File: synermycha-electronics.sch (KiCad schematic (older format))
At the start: 0 parts

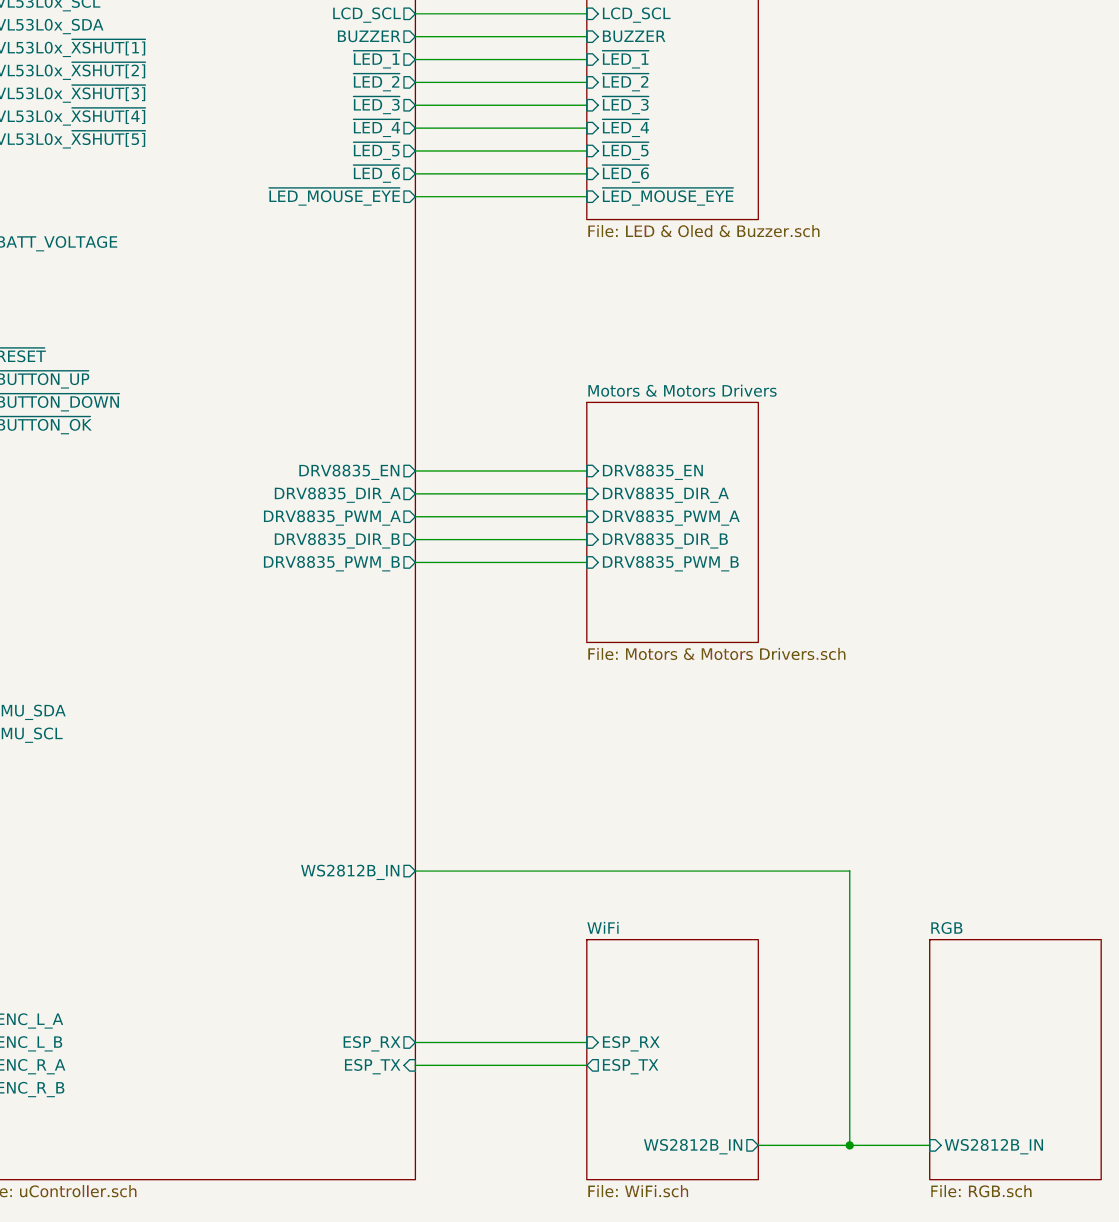
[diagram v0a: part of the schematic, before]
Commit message: Updated BT module connection, 3D models and wiring.
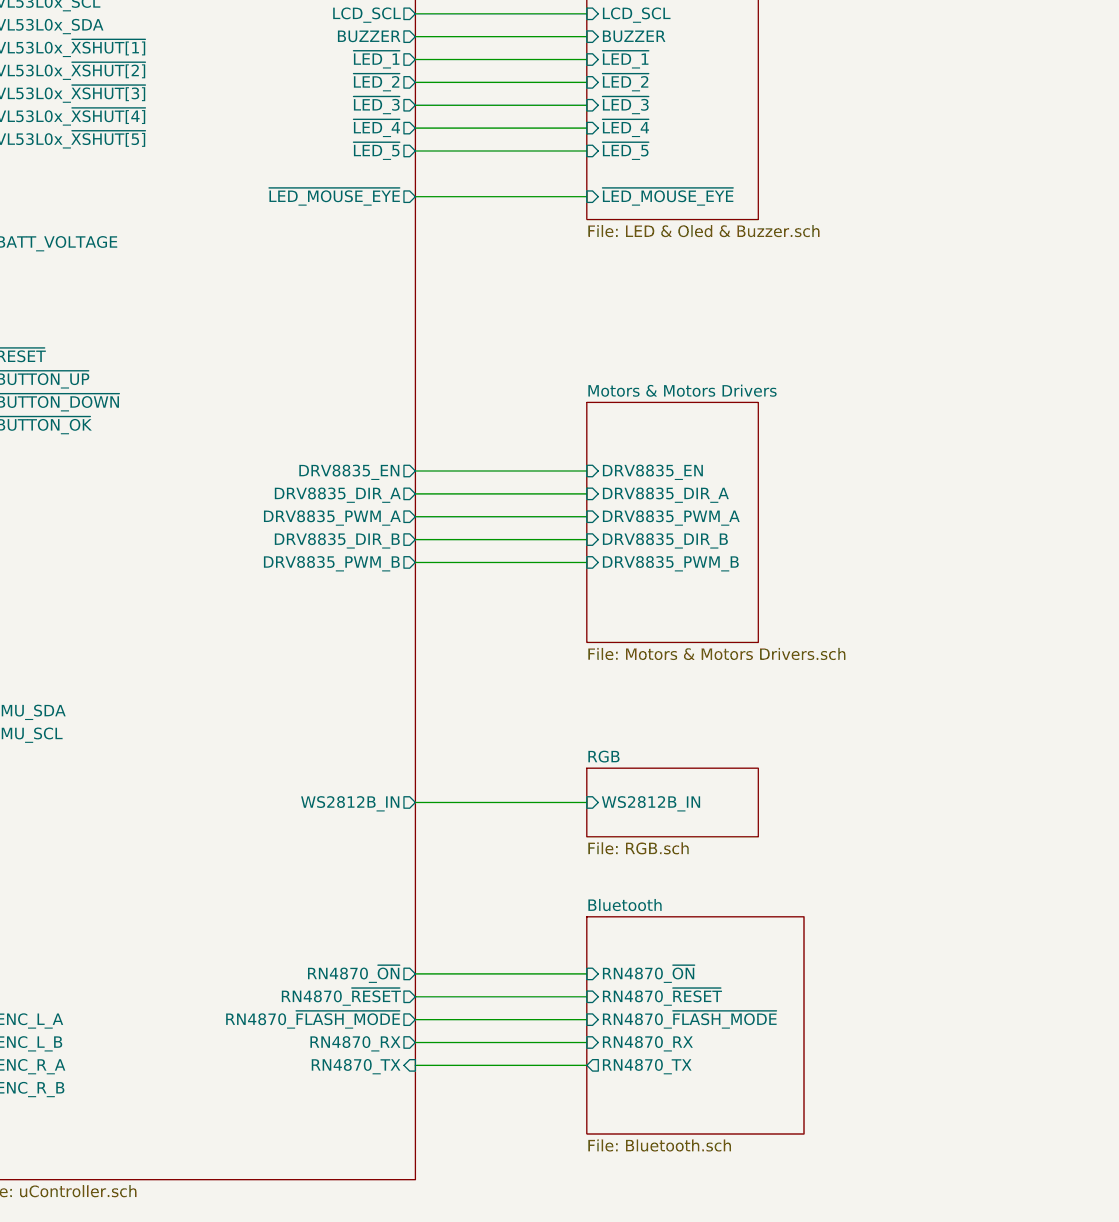
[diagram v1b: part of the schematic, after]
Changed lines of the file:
@@
 F8 "VL53L0x_~XSHUT[5]" I R 4050 1750 50
-$EndSheet
-$Sheet
-S 7350 5250 750  1050
-U 5E5F55AD
-F0 "WiFi" 50
-F1 "WiFi.sch" 50
-F2 "ESP_RX" I L 7350 5700 50
-F3 "ESP_TX" O L 7350 5800 50
-F4 "WS2812B_IN" O R 8100 6150 50
 $EndSheet
 Text Notes 1000 1150 0    50   ~ 0
@@
 F3 "IMU_SCL" I R 4050 4350 50
 $EndSheet
-$Sheet
-S 8850 5250 750  1050
-U 5E79B5DD
-F0 "RGB" 50
-F1 "RGB.sch" 50
-F2 "WS2812B_IN" I L 8850 6150 50
-$EndSheet
-Wire Wire Line
-	8100 6150 8500 6150
 Wire Wire Line
 	4050 2700 4700 2700
@@
 F15 "IMU_SDA" B L 4700 4250 50
 F16 "IMU_SCL" O L 4700 4350 50
-F17 "ESP_RX" O R 6600 5700 50
-F18 "ESP_TX" I R 6600 5800 50
+F17 "RN4870_RX" O R 6600 5700 50
+F18 "RN4870_TX" I R 6600 5800 50
 F19 "BATT_VOLTAGE" I L 4700 2200 50
 F20 "LCD_SDA" B R 6600 1100 50
@@
 F34 "VL53L0x_~XSHUT[4]" O L 4700 1650 50
 F35 "VL53L0x_~XSHUT[5]" O L 4700 1750 50
-F36 "~LED_6" O R 6600 1900 50
-F37 "WS2812B_IN" O R 6600 4950 50
+F36 "WS2812B_IN" O R 6600 4650 50
+F37 "RN4870_~ON" O R 6600 5400 50
+F38 "RN4870_~RESET" O R 6600 5500 50
+F39 "RN4870_~FLASH_MODE" O R 6600 5600 50
 $EndSheet
-Wire Wire Line
-	7350 1900 6600 1900
 Wire Wire Line
 	6600 1800 7350 1800
@@
 F9 "~LED_5" I L 7350 1800 50
 F10 "~LED_MOUSE_EYE" I L 7350 2000 50
-F11 "~LED_6" I L 7350 1900 50
 $EndSheet
 Wire Wire Line
@@
 Wire Wire Line
 	6600 2000 7350 2000
+$Sheet
+S 7350 4500 750  300
+U 5E79B5DD
+F0 "RGB" 50
+F1 "RGB.sch" 50
+F2 "WS2812B_IN" I L 7350 4650 50
+$EndSheet
 Wire Wire Line
-	6600 4950 8500 4950
+	7350 4650 6600 4650
+$Sheet
+S 7350 5150 950  950
+U 5E5F55AD
+F0 "Bluetooth" 50
+F1 "Bluetooth.sch" 50
+F2 "RN4870_RX" I L 7350 5700 50
+F3 "RN4870_TX" O L 7350 5800 50
+F4 "RN4870_~RESET" I L 7350 5500 50
+F5 "RN4870_~FLASH_MODE" I L 7350 5600 50
+F6 "RN4870_~ON" I L 7350 5400 50
+$EndSheet
 Wire Wire Line
-	8500 4950 8500 6150
-Connection ~ 8500 6150
+	7350 5600 6600 5600
 Wire Wire Line
-	8500 6150 8850 6150
+	6600 5500 7350 5500
+Wire Wire Line
+	7350 5400 6600 5400
 $EndSCHEMATC

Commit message: Zmieniono kontroler USB-PD
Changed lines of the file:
@@
 F1 "Power Section.sch" 50
 F2 "BATT_VOLTAGE" O R 1550 1350 50
+F3 "STSUSB4500_SDA" B R 1550 900 50
+F4 "STUSB_4500_SCL" I R 1550 1000 50
 $EndSheet
 $Sheet
@@
 F8 "VL53L0x_~XSHUT[5]" I R 4050 1750 50
 $EndSheet
-Text Notes 1000 1150 0    50   ~ 0
+Text Notes 650  1400 0    50   ~ 0
 6V,\n3V3\n
 $Sheet
@@
 Wire Wire Line
 	2450 2200 4700 2200
-Wire Wire Line
-	7350 1100 6600 1100
-Wire Wire Line
-	6600 1200 7350 1200
 $Sheet
 S 4700 950  1900 5350
@@
 Wire Wire Line
 	7350 5400 6600 5400
+Wire Wire Line
+	1550 1000 1750 1000
+Wire Wire Line
+	6600 1100 6900 1100
+Wire Wire Line
+	6800 800  6800 1200
+Wire Wire Line
+	6600 1200 6800 1200
+Connection ~ 6800 1200
+Wire Wire Line
+	6800 1200 7350 1200
+Wire Wire Line
+	6900 1100 6900 700
+Connection ~ 6900 1100
+Wire Wire Line
+	6900 1100 7350 1100
+Wire Wire Line
+	1550 900  1650 900
+Wire Wire Line
+	1650 700  1650 900
+Wire Wire Line
+	1650 700  6900 700
+Wire Wire Line
+	1750 1000 1750 800
+Wire Wire Line
+	1750 800  6800 800
 $EndSCHEMATC

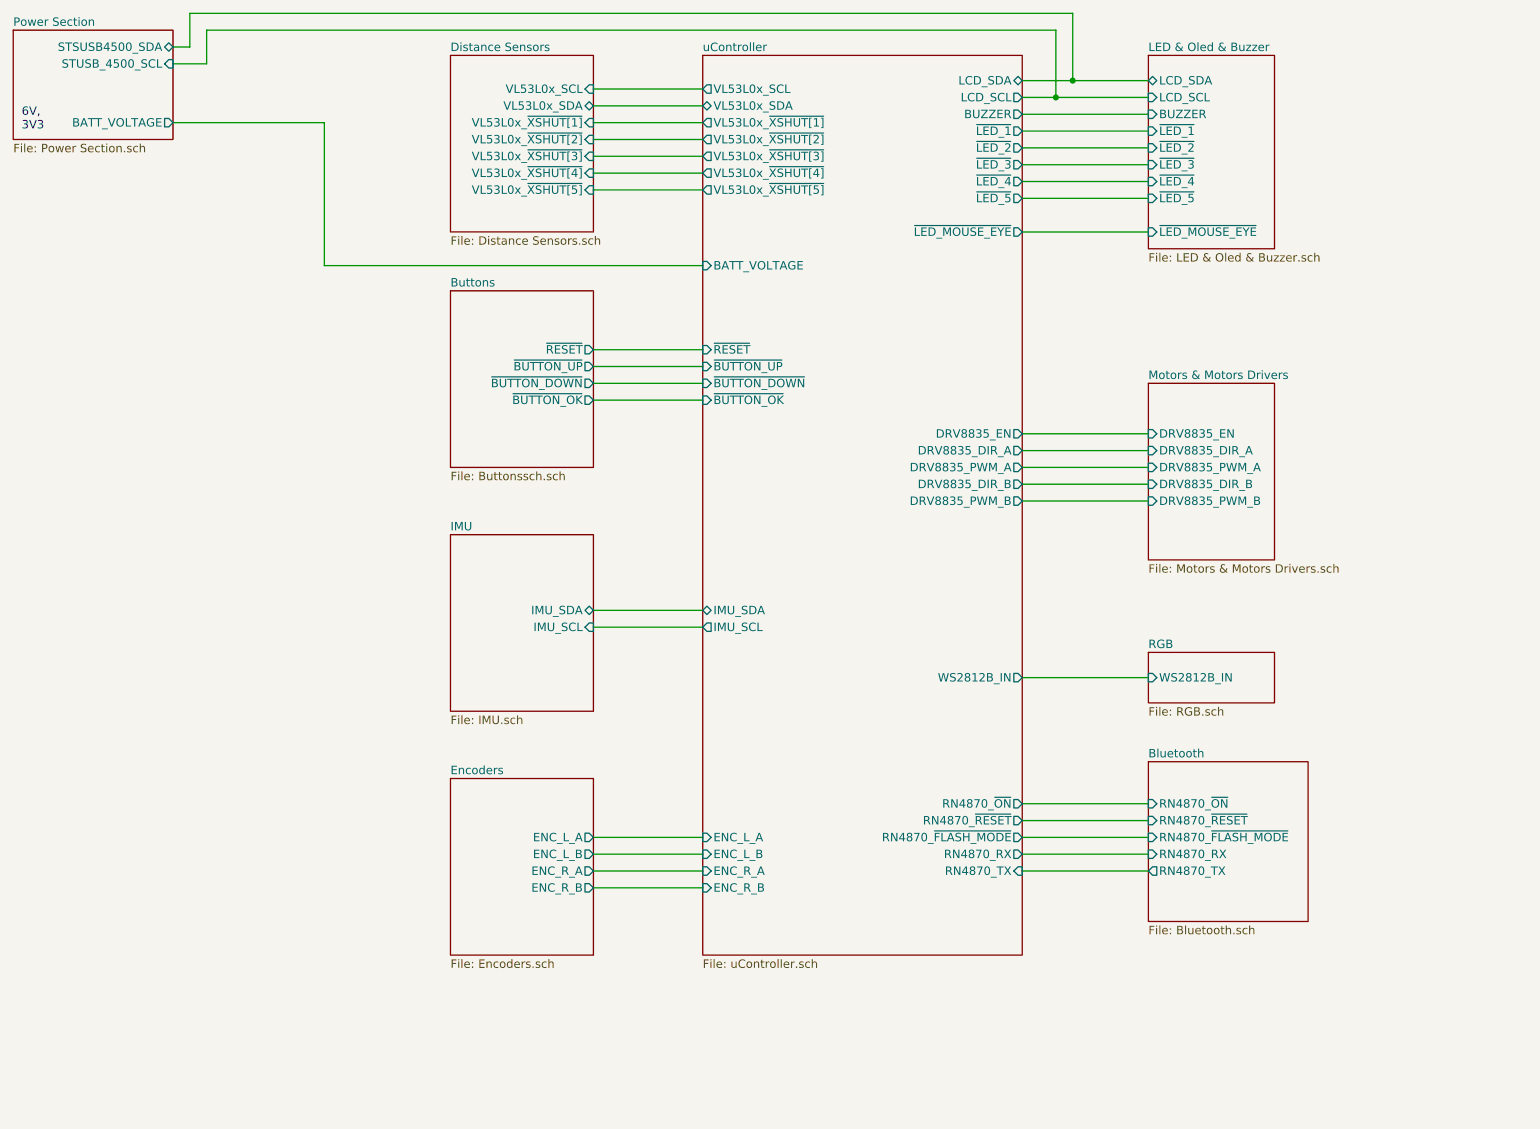
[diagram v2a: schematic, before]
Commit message: Dodano punkty testowe, poprawienie schematu
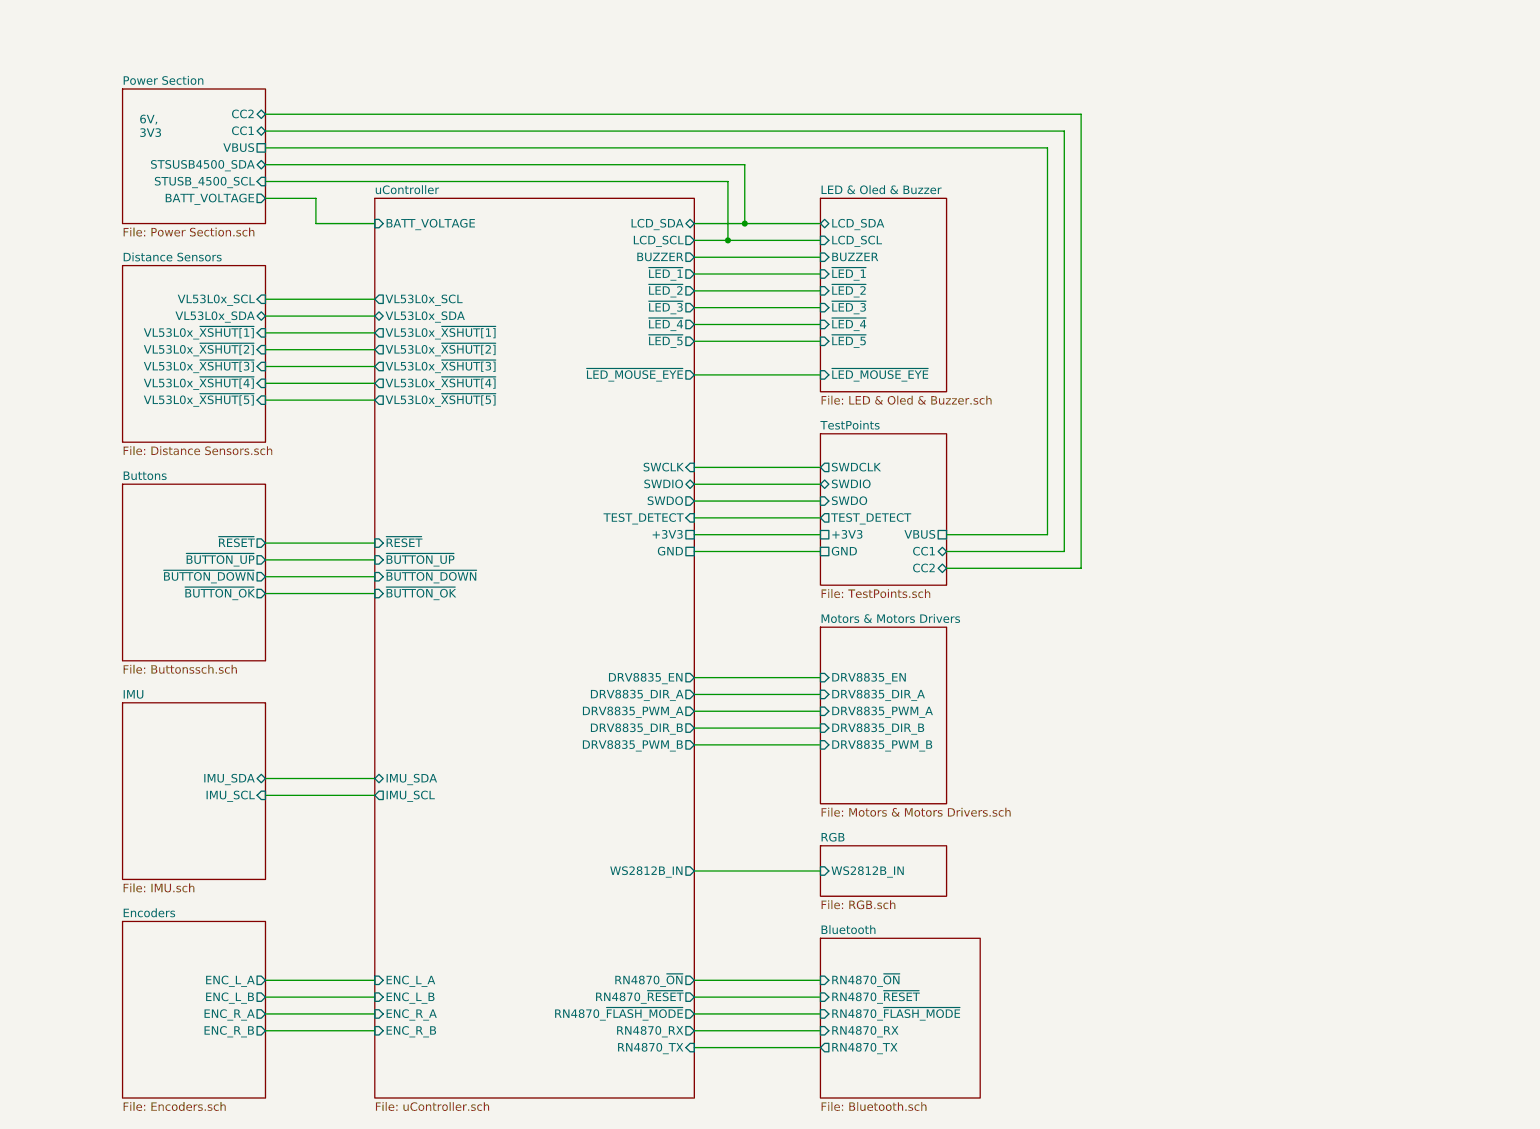
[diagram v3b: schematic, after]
